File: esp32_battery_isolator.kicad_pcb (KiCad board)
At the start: 4 copper layers, 90 x 89.9 mm, 100 parts, among them J1 Conn_01x03_Male, J2 USB_C_Receptacle_USB2.0, Q1 MMBT3904, Q10 MMBT3904, Q11 MMBT3906, Q12 AONR21357, Q13 MMBT3904, Q14 MMBT3904, Q15 MMBT3904, Q16 MMBT3906, Q17 MMBT3904, Q18 AONR21357, Q19 MMBT3904, Q2 MMBT3904, Q20 MMBT3906, Q21 AONR21357, Q3 MMBT3906, Q4 HSBA100P03, Q5 HSBA100P03, Q6 HSBA100P03, Q7 HSBA100P03, Q8 MMBT3904, Q9 MMBT3904, SW1 C620183, SW2 C620183, U1 ESP32-WROOM-32D, U10 INA219BxDCN, U2 INA219BxDCN, U3 INA219BxDCN, U4 INA219BxDCN, U5 XL1509_SOP8, U6 CH340N, U7 INA219BxDCN, U8 ADC128D818, U9 INA219BxDCN

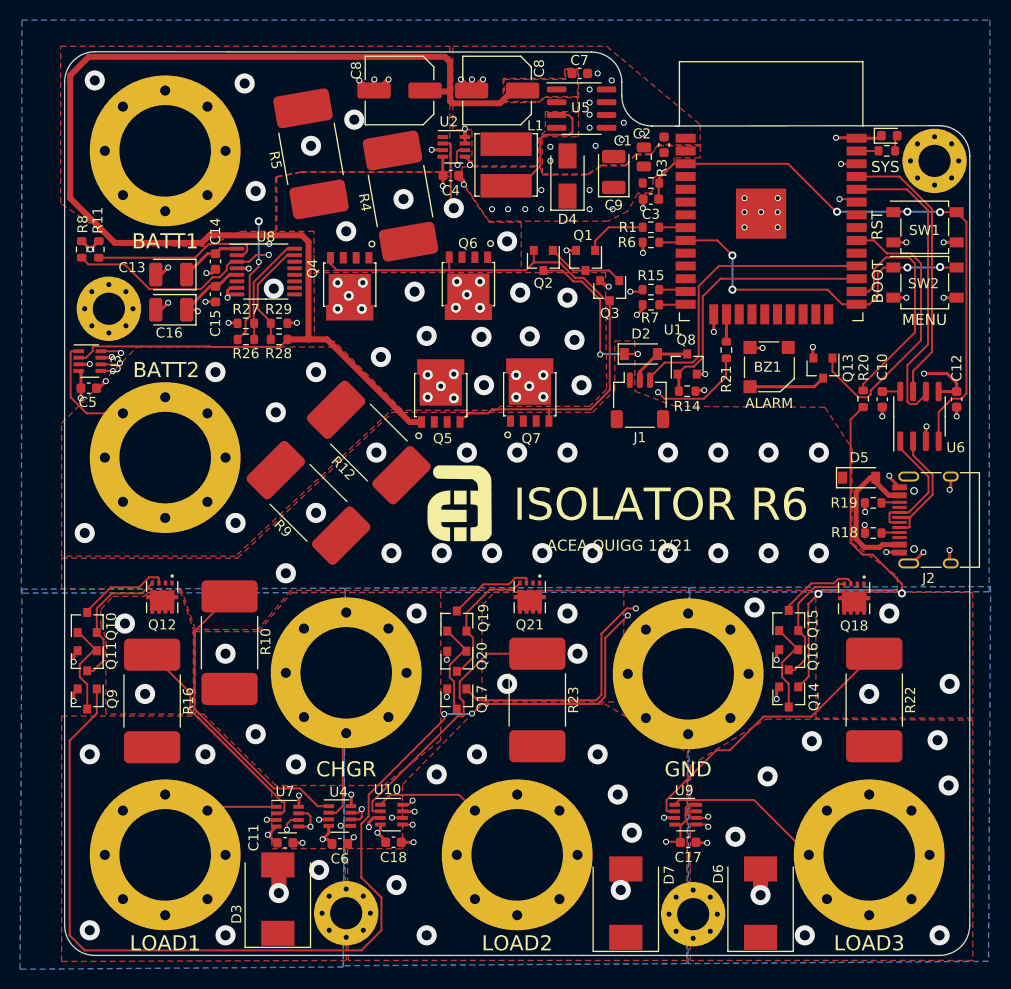
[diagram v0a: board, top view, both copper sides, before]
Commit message: Changed from push pull to independent pull up and pull down mosfets
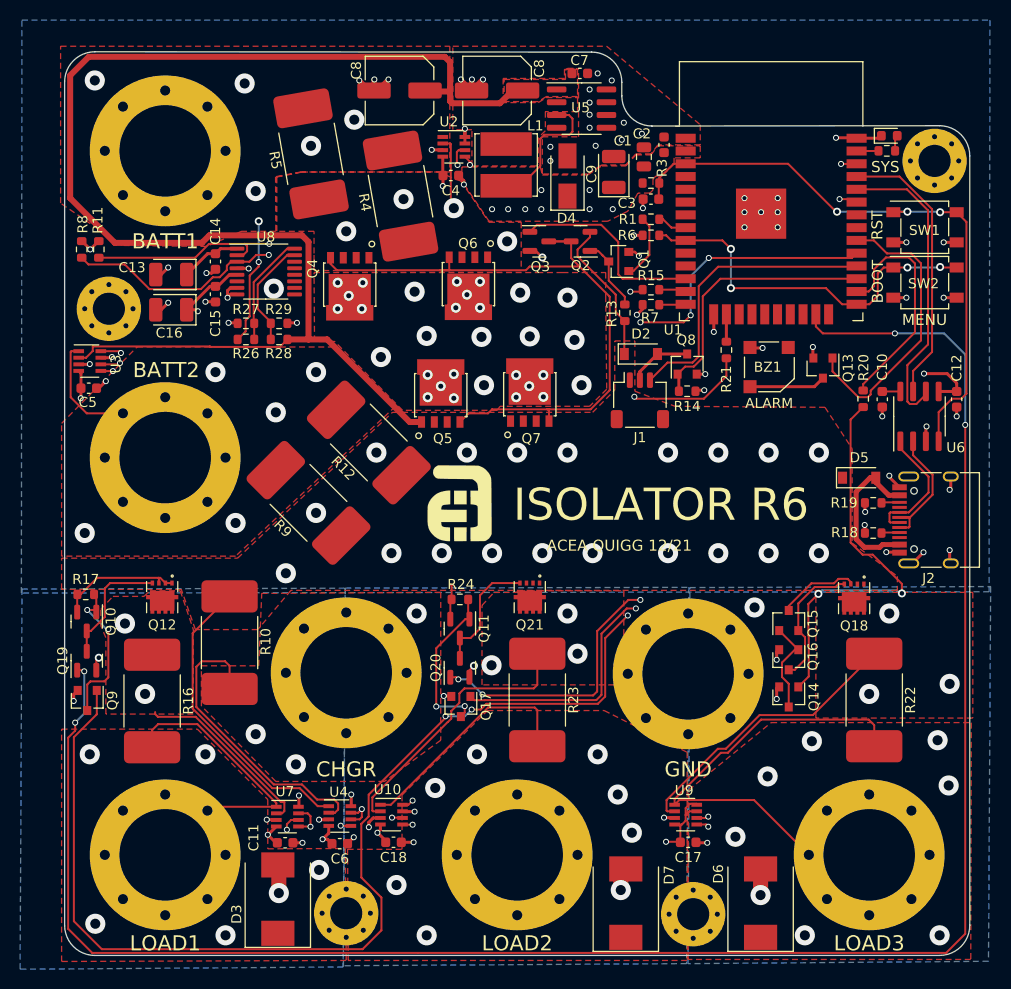
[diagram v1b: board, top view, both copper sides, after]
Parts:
- added R13: 5k, Resistor_SMD:R_0603_1608Metric, F.Cu at (163.3, 70.2)
- added R17: 5k, Resistor_SMD:R_0603_1608Metric, F.Cu at (109.8, 98.2)
- added R24: 5k, Resistor_SMD:R_0603_1608Metric, F.Cu at (146.9, 98.8)
- Q10, Q2: value MMBT3904 -> Q_PMOS_GSD
- Q11: value MMBT3906 -> Q_PMOS_GSD
- Q19: value MMBT3904 -> 2N7002
- Q20, Q3: value MMBT3906 -> 2N7002
- moved Q11 37.2 mm to (146.9, 101.7)
- moved Q19 37.0 mm to (109.8, 104.8)
- moved Q3 8.54 mm to (154.8, 63.1), turned to 0 degrees
- moved Q2 4.16 mm to (158.9, 63.1), turned to 180 degrees
- moved Q1 3.30 mm to (162.8, 65.2), turned to 180 degrees
- moved Q17 0.85 mm to (147.1, 109.4)
- moved R1 0.80 mm to (165.9, 61.0)
- moved Q20 0.72 mm to (146.9, 105.5), turned to 90 degrees
- moved R6 0.70 mm to (165.9, 62.5)
- moved Q9 0.15 mm to (109.9, 108.8)
- moved Q10 0.11 mm to (109.8, 101.0), turned to -90 degrees
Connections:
- Q1 pad 3: Net-(Q1-Pad3) -> Net-(Q2-Pad1)
- Q10 pad 2: Net-(Q10-Pad2) -> COM
- Q10 pad 3: COM -> Net-(Q12-Pad1)
- Q11 pad 1: Net-(Q10-Pad1) -> Net-(Q17-Pad3)
- Q11 pad 2: GND -> COM
- Q11 pad 3: Net-(Q10-Pad2) -> Net-(Q21-Pad1)
- Q12 pad 1: Net-(Q10-Pad2) -> Net-(Q12-Pad1)
- Q19 pad 1: Net-(Q17-Pad3) -> L1ON
- Q19 pad 2: Net-(Q19-Pad2) -> GND
- Q19 pad 3: COM -> Net-(Q12-Pad1)
- Q2 pad 1: Net-(Q1-Pad3) -> Net-(Q2-Pad1)
- Q2 pad 2: G -> COM
- Q2 pad 3: COM -> G
- Q20 pad 1: Net-(Q17-Pad3) -> L2ON
- Q20 pad 3: Net-(Q19-Pad2) -> Net-(Q21-Pad1)
- Q21 pad 1: Net-(Q19-Pad2) -> Net-(Q21-Pad1)
- Q3 pad 1: Net-(Q1-Pad3) -> B1ON
- Q4 pad 2: D -> Net-(Q4-Pad2)
- Q5 pad 2: D -> Net-(Q4-Pad2)
- R1 pad 1: B1ON -> B1OFF
- R15 pad 1: L1ON -> L1OFF
- R21 pad 1: L2ON -> L2OFF
- U1 pad 12: unconnected-(U1-Pad12) -> B1ON
- U1 pad 13: L1ON -> L1OFF
- U1 pad 16: L2ON -> L2OFF
- U1 pad 23: unconnected-(U1-Pad23) -> L1ON
- U1 pad 29: unconnected-(U1-Pad29) -> L2ON
- U1 pad 8: B1ON -> B1OFF
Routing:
- net L1ON: track 2.70 -> 192.8 mm, vias 0 -> 4
- net L2ON: track 2.72 -> 81.3 mm, vias 0 -> 6
- net LOAD3: track 15.8 -> 41.8 mm
- net Net-(H3-Pad1): track 9.06 -> 30.2 mm, vias 4 -> 3
- net LOAD1: track 7.01 -> 24.9 mm
- net B1ON: track 2.64 -> 19.9 mm
- net Net-(Q10-Pad2): track 14.1 -> 0.00 mm
- net Net-(Q19-Pad2): track 13.4 -> 0.00 mm
- net LOAD2: track 10.5 -> 23.3 mm
- net Net-(Q21-Pad1): track 0.00 -> 12.2 mm
- net Net-(Q12-Pad1): track 0.00 -> 12.2 mm
- net Net-(Q1-Pad3): track 7.84 -> 0.00 mm
- net Net-(Q2-Pad1): track 0.00 -> 7.30 mm
- net Net-(Q17-Pad3): track 9.68 -> 16.4 mm, vias 0 -> 2
- net Net-(Q10-Pad1): track 9.66 -> 15.5 mm, vias 0 -> 2
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
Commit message: Merged Vincent's changes
Also modified a few tracks, routes and pours
Cleaned up the DRC
Fixed clearances
Found an issue with Q4 and Q5
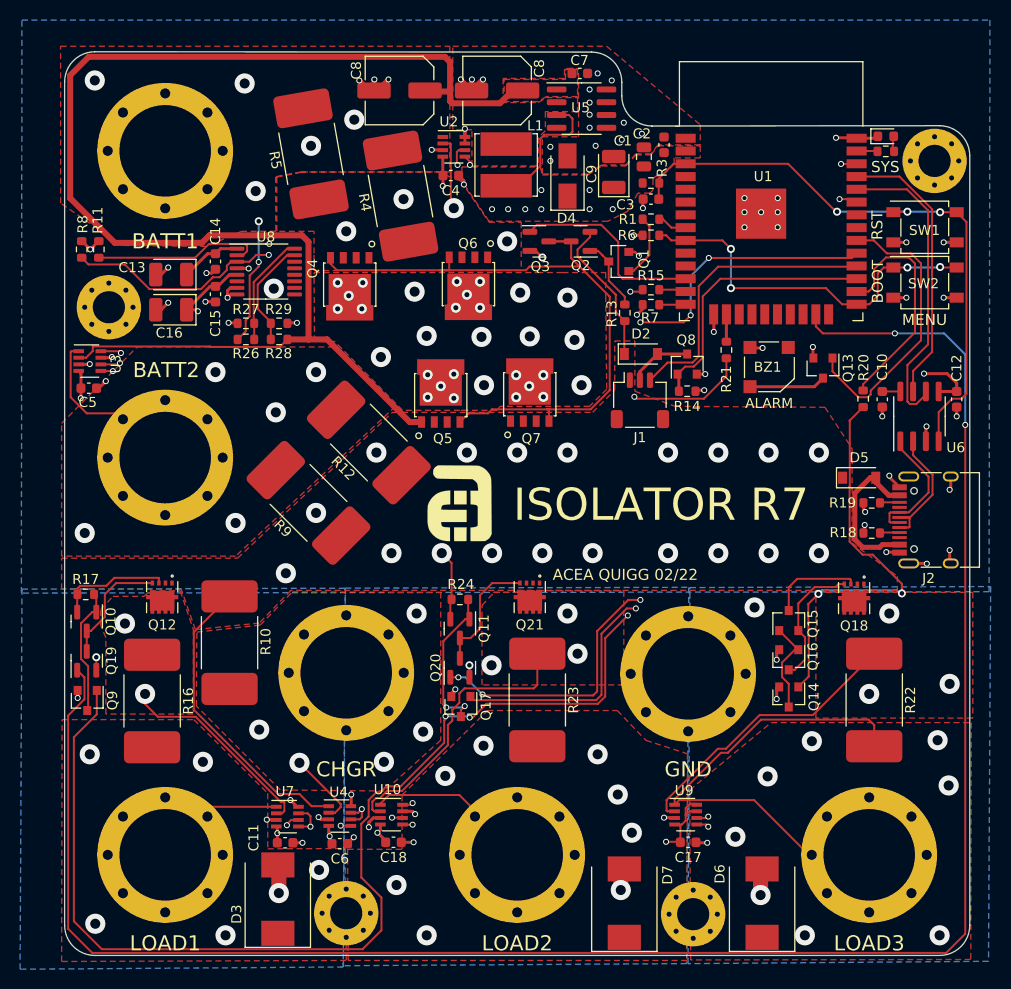
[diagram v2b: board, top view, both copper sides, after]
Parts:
- moved D1 0.35 mm to (189.3, 52.7)
- moved D6 0.15 mm to (177.0, 128.9)
- moved R18 0.15 mm to (187.9, 92.2)
- moved R19 0.15 mm to (187.9, 89.2)
- moved H12 0.15 mm to (112.0, 69.7)
- moved D7 0.15 mm to (163.3, 128.9)
- moved R2 0.11 mm to (189.3, 54.2)
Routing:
- net Net-(H3-Pad1): track 30.2 -> 7.52 mm, vias 3 -> 5
- net LOAD1: track 24.9 -> 7.01 mm
- net LOAD2: track 23.3 -> 10.5 mm
- net COM: track 208.9 -> 212.3 mm
- net Net-(Q10-Pad1): track 15.5 -> 12.8 mm, vias 2 -> 0
- net Net-(Q12-Pad2): track 18.5 -> 20.7 mm
- net +3V3: track 56.2 -> 54.5 mm
- net Net-(Q9-Pad1): track 141.3 -> 142.4 mm
- net Net-(Q21-Pad2): track 27.3 -> 28.3 mm
- net Net-(Q17-Pad3): track 16.4 -> 15.3 mm
- net GND: track 88.4 -> 87.7 mm
- net L1ON: track 192.8 -> 192.5 mm, vias 4 -> 2
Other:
- board text added: "ACEA QUIGG 02/22"
- board text added: "ISOLATOR R7"
- board text removed: "ACEA QUIGG 12/21"
- board text removed: "ISOLATOR R6"

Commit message: More cleanup
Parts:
- removed the C8 at (140.9, 48.1)
- added C19: 100uF(220uF), Capacitor_SMD:C_Elec_6.3x5.4, F.Cu at (141.0, 48.2)
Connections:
- Q4 pad 2: Net-(Q4-Pad2) -> D
- Q5 pad 2: Net-(Q4-Pad2) -> D
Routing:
- net Net-(Q4-Pad2): vias 10 -> 0
- net D: vias 21 -> 31

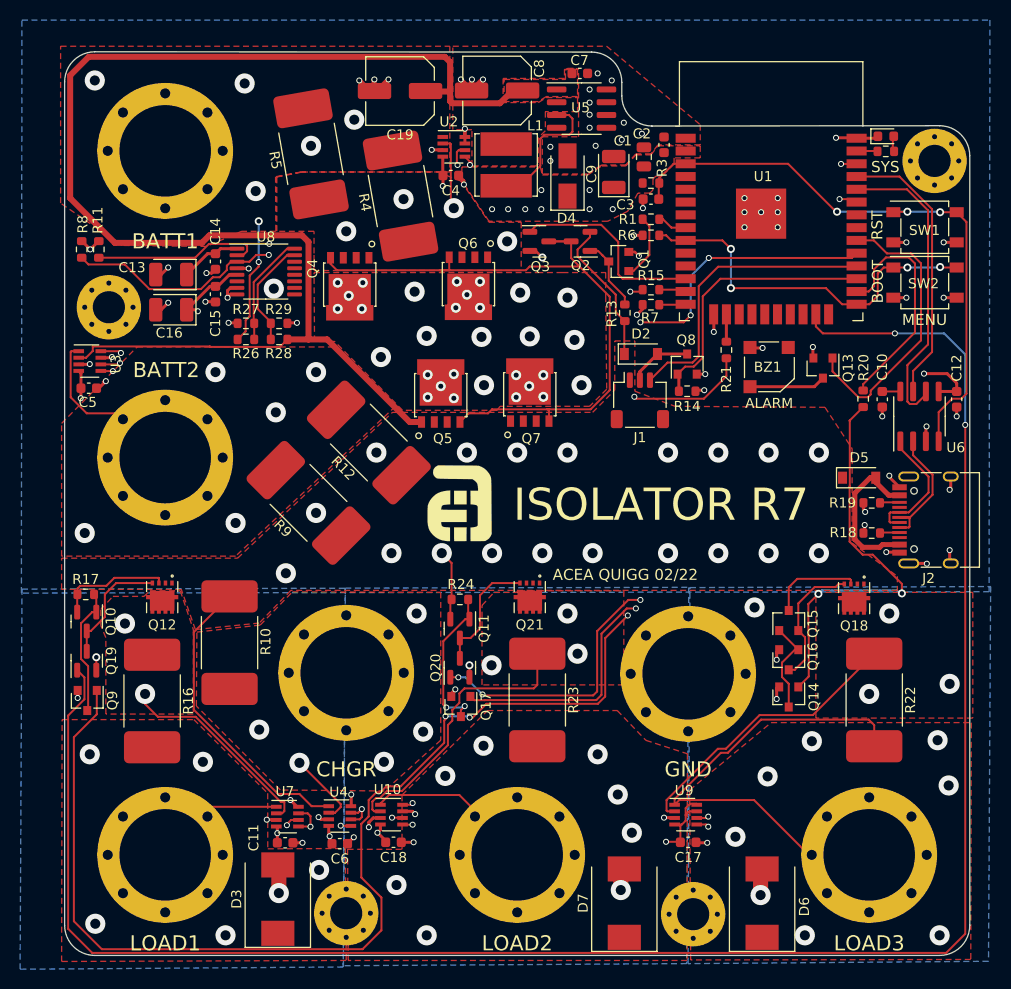
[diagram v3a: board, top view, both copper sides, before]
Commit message: More cleanup
Fixed all DRC errors
Reverted to the 4 wire method of current sensing
Switched a heap of parts to the newest versions
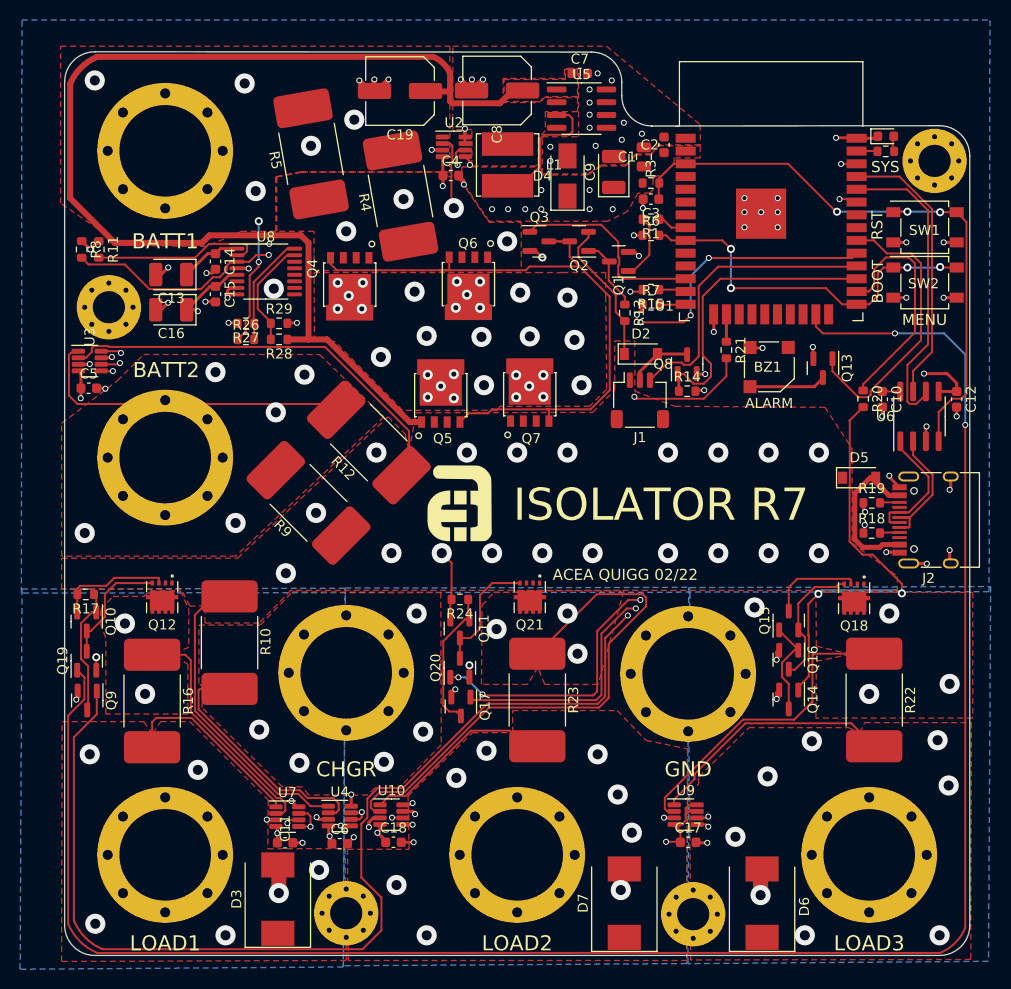
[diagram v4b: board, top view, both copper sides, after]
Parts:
- moved Q14 0.25 mm to (179.7, 108.7)
- moved L1 0.15 mm to (151.7, 55.5)
- moved Q2 0.15 mm to (158.8, 63.1)
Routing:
- net Net-(Q21-D): track 28.3 -> 54.5 mm
- net B2VM: track 11.2 -> 33.4 mm
- net COM: track 212.3 -> 231.9 mm
- net Net-(U4-IN-): track 7.52 -> 24.6 mm
- net LOAD3: track 41.8 -> 24.8 mm
- net LOAD1: track 7.01 -> 18.9 mm
- net LOAD2: track 10.5 -> 19.3 mm
- net Net-(Q12-D): track 20.7 -> 24.1 mm
- net Net-(Q18-D): track 28.6 -> 31.6 mm
- net FANON: track 27.0 -> 30.1 mm
- net Net-(Q9-B): track 142.4 -> 141.1 mm, vias 4 -> 2
- net Net-(Q11-G): track 15.3 -> 14.1 mm, vias 2 -> 0
- net SDA: track 254.4 -> 253.5 mm
- net +3V3: track 54.5 -> 54.0 mm
